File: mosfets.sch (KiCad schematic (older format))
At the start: 51 parts, among them J11 Conn_01x02, J12 Conn_01x02, J13 Conn_01x02, J14 Conn_01x02, J16 Conn_01x02, J17 Conn_01x02, J18 Conn_01x02, J19 Conn_01x02, J20 Conn_01x02, J44 Conn_01x02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

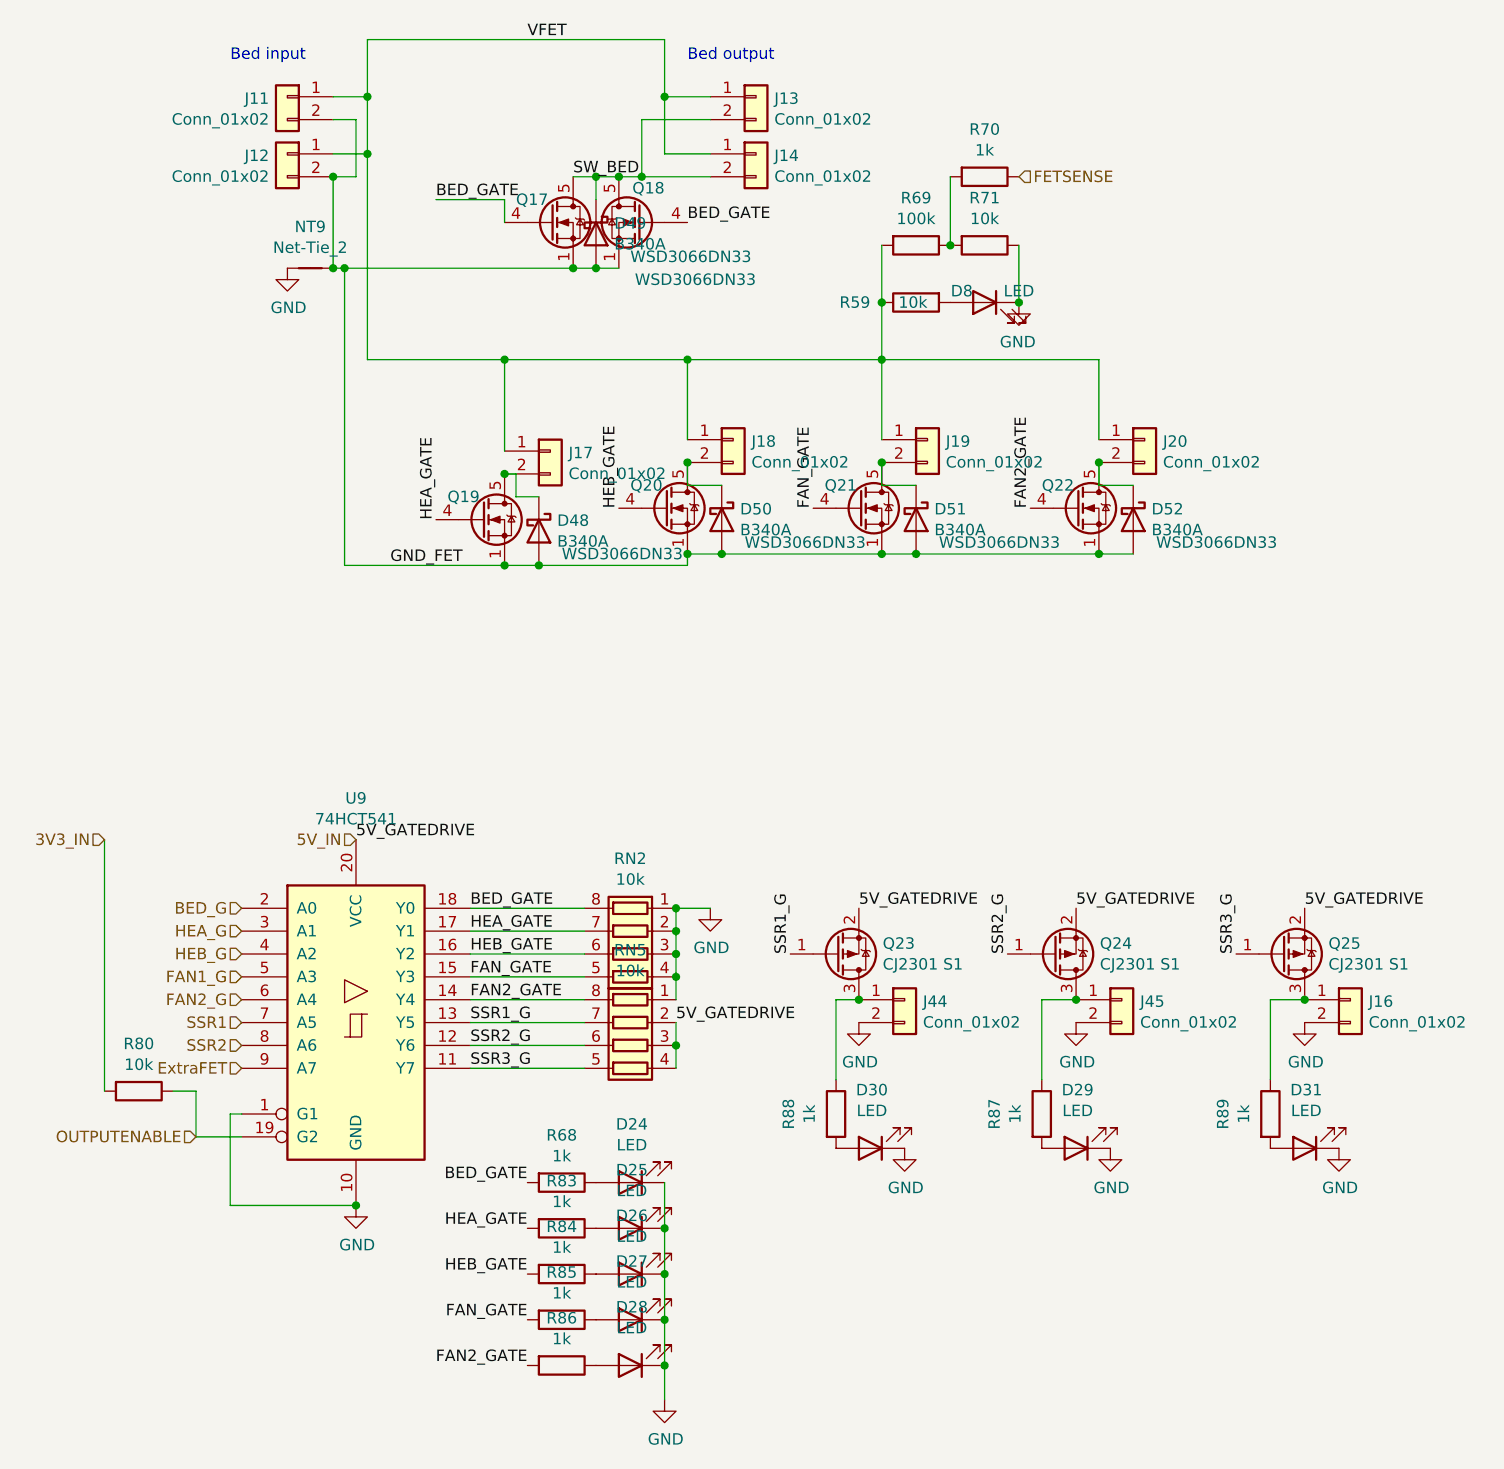
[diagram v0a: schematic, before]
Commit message: Add pfet to switch vfet positive rail and nfet to switch pfet for emergency heater poweroff.
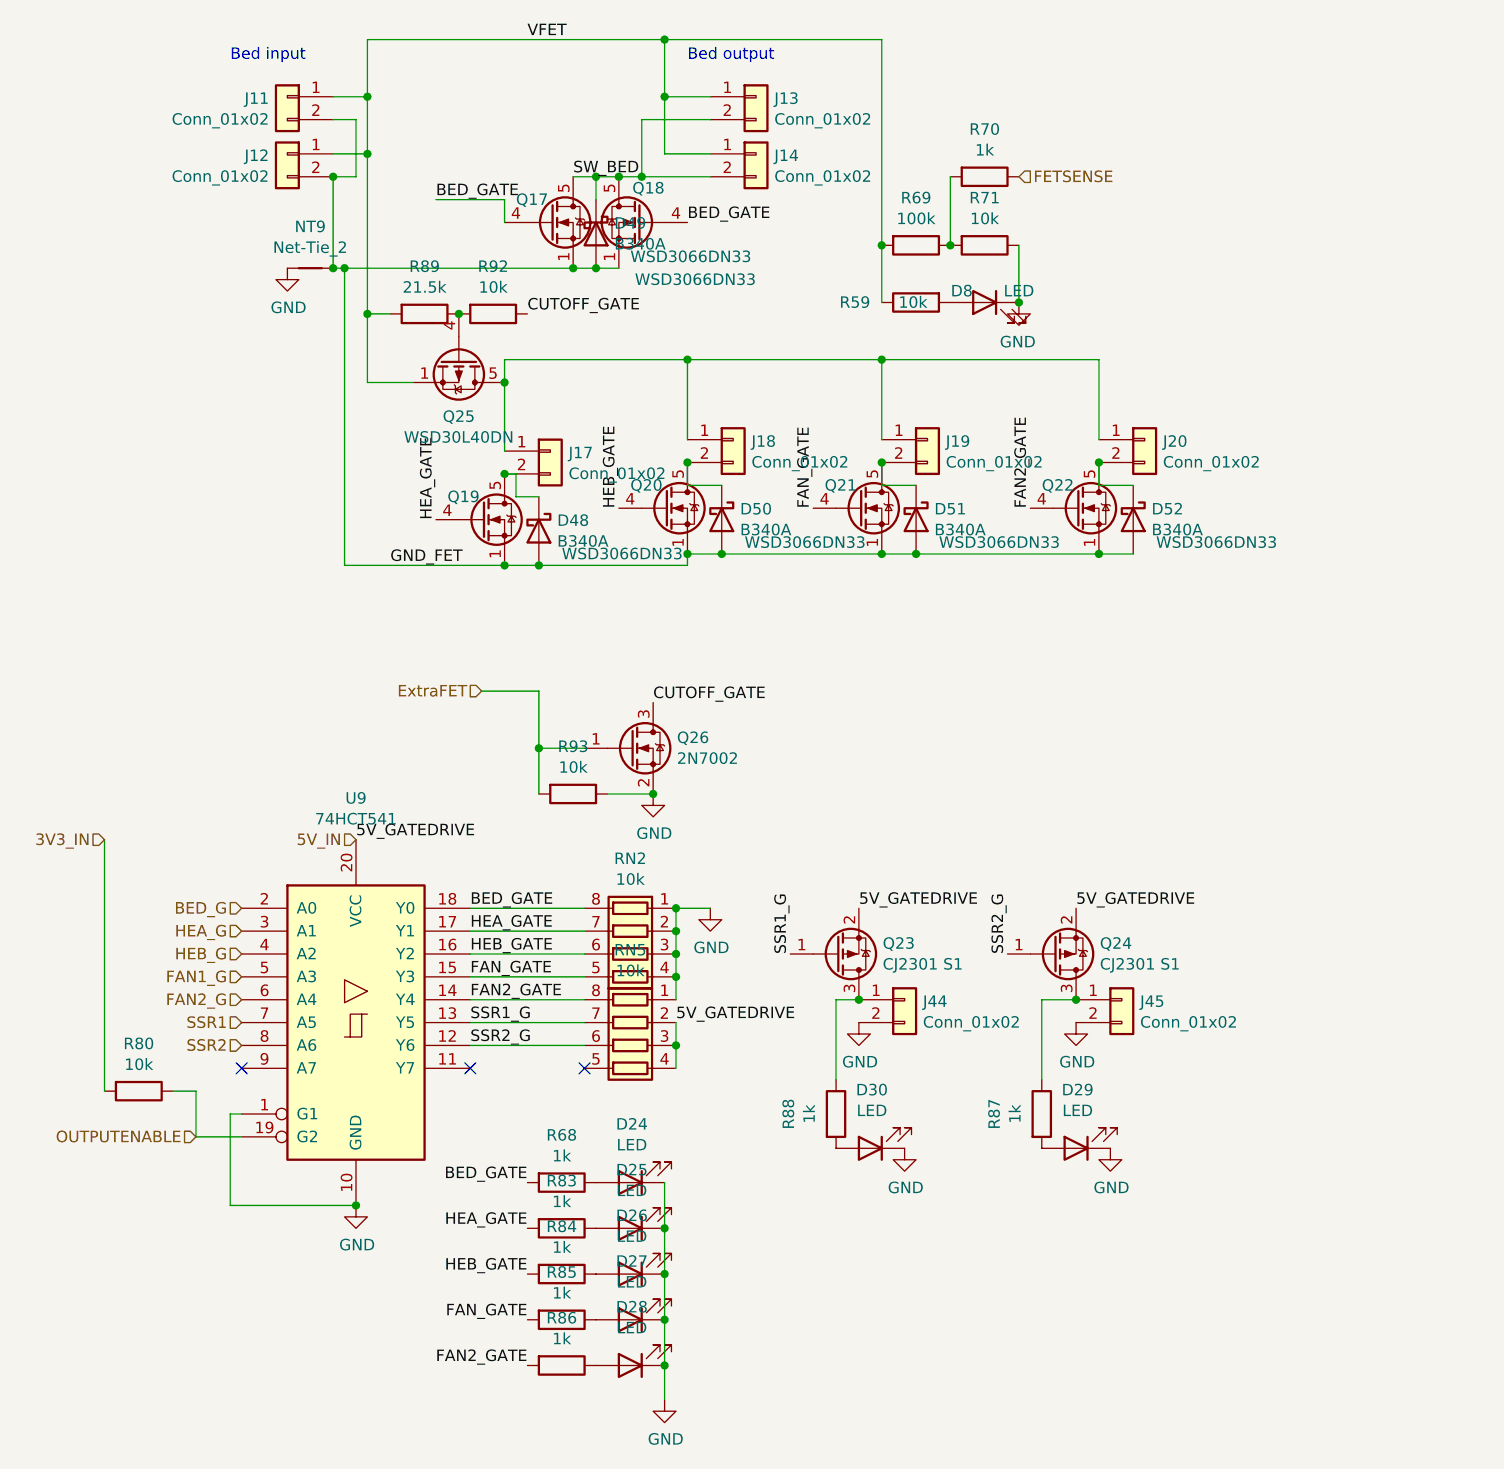
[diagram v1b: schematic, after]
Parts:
- removed D31: LED, LED_SMD:LED_0603_1608Metric, symbol Device:LED
- removed J16: Conn_01x02, Connector_PinHeader_2.54mm:PinHeader_1x02_P2.54mm_Vertical, symbol Connector_Generic:Conn_01x02
- removed Q25: CJ2301 S1, Package_TO_SOT_SMD:SOT-23, symbol Transistor_FET:AO3401A
- added Q25: WSD30L40DN, Package_SO:Vishay_PowerPAK_1212-8_Single, symbol Transistor_FET:SiS415DNT
- added Q26: 2N7002, Package_TO_SOT_SMD:SOT-23, symbol Transistor_FET:2N7002
- added R92, R93: 10k, Resistor_SMD:R_0402_1005Metric, symbol Device:R
- R89: value 1k -> 21.5k
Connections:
- net ExtraFET: now also Q26.1 (G), R93.2; no longer U9.9 (A7)
- net GND: now also Q26.2 (S), R93.1
- net VFET: now also R89.2, Q25.1 (S), Q25.2 (S), Q25.3 (S); no longer J17.1 (Pin_1), J18.1 (Pin_1), J19.1 (Pin_1), J20.1 (Pin_1)
- net at R89.1: now also Q25.4 (G), R92.2
- net SSR3_G: no longer names the net of U9.11 (Y7)
- net SSR3_G: no longer RN5.5 (R4.2)
- new net: J17.1 (Pin_1), J18.1 (Pin_1), J19.1 (Pin_1), J20.1 (Pin_1), Q25.5 (D)
- new net CUTOFF_GATE: Q26.3 (D), R92.1
- no-connect marks 0 -> 3
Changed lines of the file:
@@
 	3400 2600 2600 2600
 Wire Wire Line
-	2600 3000 2600 2600
+	2600 3000 2600 2700
 Wire Wire Line
 	2600 3500 2750 3500
@@
 Text HLabel 1450 5600 0    50   Input ~ 0
 SSR2
-Text HLabel 1450 5700 0    50   Input ~ 0
+Text HLabel 2500 4050 0    50   Input ~ 0
 ExtraFET
 Wire Wire Line
@@
 Wire Wire Line
 	2950 5600 2450 5600
-Wire Wire Line
-	2950 5700 2450 5700
 $Comp
 L Device:R R?
@@
 	-1   0    0    -1
 $EndComp
-Wire Wire Line
-	4250 2350 4250 2600
 $Comp
 L Device:R R69
@@
 Wire Wire Line
 	4250 2100 4250 2350
-Connection ~ 4250 2350
 $Comp
 L Device:R R70
@@
 Wire Wire Line
 	1900 2200 2900 2200
-Wire Wire Line
-	2600 2600 2000 2600
-Wire Wire Line
-	2000 2600 2000 1700
-Connection ~ 2600 2600
 Connection ~ 2000 1700
 Text Label 2700 1200 0    50   ~ 0
@@
 Text Label 2100 3500 0    50   ~ 0
 GND_FET
-$Comp
-L Transistor_FET:AO3401A Q25
-U 1 1 65BEA16F
-P 6000 5200
-F 0 "Q25" H 6204 5154 50  0000 L CNN
-F 1 "CJ2301 S1" H 6204 5245 50  0000 L CNN
-F 2 "Package_TO_SOT_SMD:SOT-23" H 6200 5125 50  0001 L CIN
-F 3 "http://www.aosmd.com/pdfs/datasheet/AO3401A.pdf" H 6000 5200 50  0001 L CNN
-	1    6000 5200
-	1    0    0    1
-$EndComp
-Text Label 6100 5000 0    50   ~ 0
-5V_GATEDRIVE
-$Comp
-L Connector_Generic:Conn_01x02 J?
-U 1 1 65BEA31E
-P 6300 5400
-AR Path="/65BEA31E" Ref="J?"  Part="1"
-AR Path="/612538A5/65BEA31E" Ref="J16"  Part="1"
-F 0 "J16" H 6380 5392 50  0000 L CNN
-F 1 "Conn_01x02" H 6380 5301 50  0000 L CNN
-F 2 "Connector_PinHeader_2.54mm:PinHeader_1x02_P2.54mm_Vertical" H 6300 5400 50  0001 C CNN
-F 3 "~" H 6300 5400 50  0001 C CNN
-	1    6300 5400
-	1    0    0    -1
-$EndComp
-$Comp
-L power:GND #PWR08
-U 1 1 65BEA328
-P 6100 5500
-F 0 "#PWR08" H 6100 5250 50  0001 C CNN
-F 1 "GND" H 6105 5327 50  0000 C CNN
-F 2 "" H 6100 5500 50  0001 C CNN
-F 3 "" H 6100 5500 50  0001 C CNN
-	1    6100 5500
-	1    0    0    -1
-$EndComp
-Text Label 5800 5200 1    50   ~ 0
-SSR3_G
-Text Label 2450 5700 0    50   ~ 0
-SSR3_G
 Text Label 2700 6200 2    50   ~ 0
 BED_GATE
@@
 	4050 5400 4050 5750
 Connection ~ 4150 5400
-$Comp
-L Device:R R89
-U 1 1 60EB4240
-P 5950 5900
-F 0 "R89" V 5743 5900 50  0000 C CNN
-F 1 "1k" V 5834 5900 50  0000 C CNN
-F 2 "Resistor_SMD:R_0402_1005Metric" V 5880 5900 50  0001 C CNN
-F 3 "~" H 5950 5900 50  0001 C CNN
-	1    5950 5900
-	1    0    0    -1
-$EndComp
-$Comp
-L Device:LED D31
-U 1 1 60EB44E2
-P 6100 6050
-F 0 "D31" H 6093 5795 50  0000 C CNN
-F 1 "LED" H 6093 5886 50  0000 C CNN
-F 2 "LED_SMD:LED_0603_1608Metric" H 6100 6050 50  0001 C CNN
-F 3 "~" H 6100 6050 50  0001 C CNN
-	1    6100 6050
-	-1   0    0    1
-$EndComp
-$Comp
-L power:GND #PWR067
-U 1 1 60EB44EC
-P 6250 6050
-F 0 "#PWR067" H 6250 5800 50  0001 C CNN
-F 1 "GND" H 6255 5877 50  0000 C CNN
-F 2 "" H 6250 6050 50  0001 C CNN
-F 3 "" H 6250 6050 50  0001 C CNN
-	1    6250 6050
-	1    0    0    -1
-$EndComp
-Wire Wire Line
-	6100 5400 5950 5400
-Wire Wire Line
-	5950 5400 5950 5750
-Connection ~ 6100 5400
 Wire Wire Line
 	3350 5700 3350 5600
@@
 Wire Wire Line
 	3000 2200 2900 2200
+NoConn ~ 1450 5700
+Wire Wire Line
+	4250 2100 4250 1200
+Wire Wire Line
+	4250 1200 3300 1200
+Connection ~ 4250 2100
+Connection ~ 3300 1200
+$Comp
+L Transistor_FET:SiS415DNT Q25
+U 1 1 610823DA
+P 2400 2600
+F 0 "Q25" V 2649 2600 50  0000 C CNN
+F 1 "WSD30L40DN" V 2740 2600 50  0000 C CNN
+F 2 "Package_SO:Vishay_PowerPAK_1212-8_Single" H 2600 2525 50  0001 L CIN
+F 3 "https://www.vishay.com/docs/63684/sis415dnt.pdf" V 2400 2600 50  0001 L CNN
+	1    2400 2600
+	0    1    1    0
+$EndComp
+Connection ~ 2600 2700
+Wire Wire Line
+	2600 2700 2600 2600
+Wire Wire Line
+	2200 2700 2000 2700
+Wire Wire Line
+	2000 1700 2000 2400
+$Comp
+L Device:R R89
+U 1 1 6108A26A
+P 2250 2400
+F 0 "R89" V 2043 2400 50  0000 C CNN
+F 1 "21.5k" V 2134 2400 50  0000 C CNN
+F 2 "Resistor_SMD:R_0402_1005Metric" V 2180 2400 50  0001 C CNN
+F 3 "~" H 2250 2400 50  0001 C CNN
+	1    2250 2400
+	0    1    1    0
+$EndComp
+Wire Wire Line
+	2100 2400 2000 2400
+Connection ~ 2000 2400
+Wire Wire Line
+	2000 2400 2000 2700
+Text Label 2700 2400 0    50   ~ 0
+CUTOFF_GATE
+Text Label 3250 4100 0    50   ~ 0
+CUTOFF_GATE
+$Comp
+L Device:R R92
+U 1 1 610A49E0
+P 2550 2400
+F 0 "R92" V 2343 2400 50  0000 C CNN
+F 1 "10k" V 2434 2400 50  0000 C CNN
+F 2 "Resistor_SMD:R_0402_1005Metric" V 2480 2400 50  0001 C CNN
+F 3 "~" H 2550 2400 50  0001 C CNN
+	1    2550 2400
+	0    1    1    0
+$EndComp
+Connection ~ 2400 2400
+NoConn ~ 2950 5700
+NoConn ~ 2450 5700
+$Comp
+L Transistor_FET:2N7002 Q26
+U 1 1 610B28F1
+P 3150 4300
+F 0 "Q26" H 3354 4346 50  0000 L CNN
+F 1 "2N7002" H 3354 4255 50  0000 L CNN
+F 2 "Package_TO_SOT_SMD:SOT-23" H 3350 4225 50  0001 L CIN
+F 3 "https://www.onsemi.com/pub/Collateral/NDS7002A-D.PDF" H 3150 4300 50  0001 L CNN
+	1    3150 4300
+	1    0    0    -1
+$EndComp
+$Comp
+L power:GND #PWR08
+U 1 1 610B5CC2
+P 3250 4500
+F 0 "#PWR08" H 3250 4250 50  0001 C CNN
+F 1 "GND" H 3255 4327 50  0000 C CNN
+F 2 "" H 3250 4500 50  0001 C CNN
+F 3 "" H 3250 4500 50  0001 C CNN
+	1    3250 4500
+	1    0    0    -1
+$EndComp
+$Comp
+L Device:R R93
+U 1 1 610B7D0D
+P 2900 4500
+F 0 "R93" V 2693 4500 50  0000 C CNN
+F 1 "10k" V 2784 4500 50  0000 C CNN
+F 2 "Resistor_SMD:R_0402_1005Metric" V 2830 4500 50  0001 C CNN
+F 3 "~" H 2900 4500 50  0001 C CNN
+	1    2900 4500
+	0    1    1    0
+$EndComp
+Wire Wire Line
+	2950 4300 2750 4300
+Wire Wire Line
+	2750 4300 2750 4500
+Wire Wire Line
+	3250 4500 3050 4500
+Connection ~ 3250 4500
+Wire Wire Line
+	2500 4050 2750 4050
+Wire Wire Line
+	2750 4050 2750 4300
+Connection ~ 2750 4300
 $EndSCHEMATC

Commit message: Fix FPs for U4 and U9
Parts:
- U9: footprint Package_SO:TSSOP-20_4.4x5mm_P0.5mm -> Package_SO:TSSOP-20_4.4x6.5mm_P0.65mm
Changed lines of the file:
@@
 F 0 "U9" H 1950 6481 50  0000 C CNN
 F 1 "74HCT541" H 1950 6390 50  0000 C CNN
-F 2 "Package_SO:TSSOP-20_4.4x5mm_P0.5mm" H 1950 5500 50  0001 C CNN
+F 2 "Package_SO:TSSOP-20_4.4x6.5mm_P0.65mm" H 1950 5500 50  0001 C CNN
 F 3 "http://www.ti.com/lit/gpn/sn74HCT541" H 1950 5500 50  0001 C CNN
 	1    1950 5500

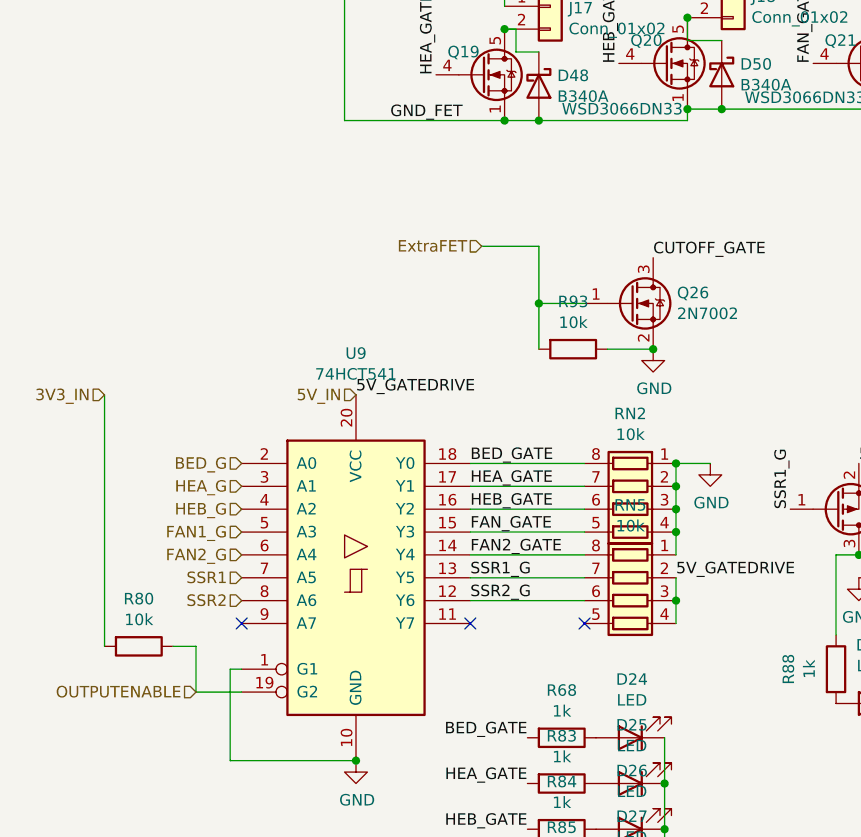
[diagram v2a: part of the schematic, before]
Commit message: Switch ADC opamp to 5V Add 4.7k series resistors (RN9) to thermistor inputs. Add 10k pulldowns (RN8) to FET gate driver inputs.
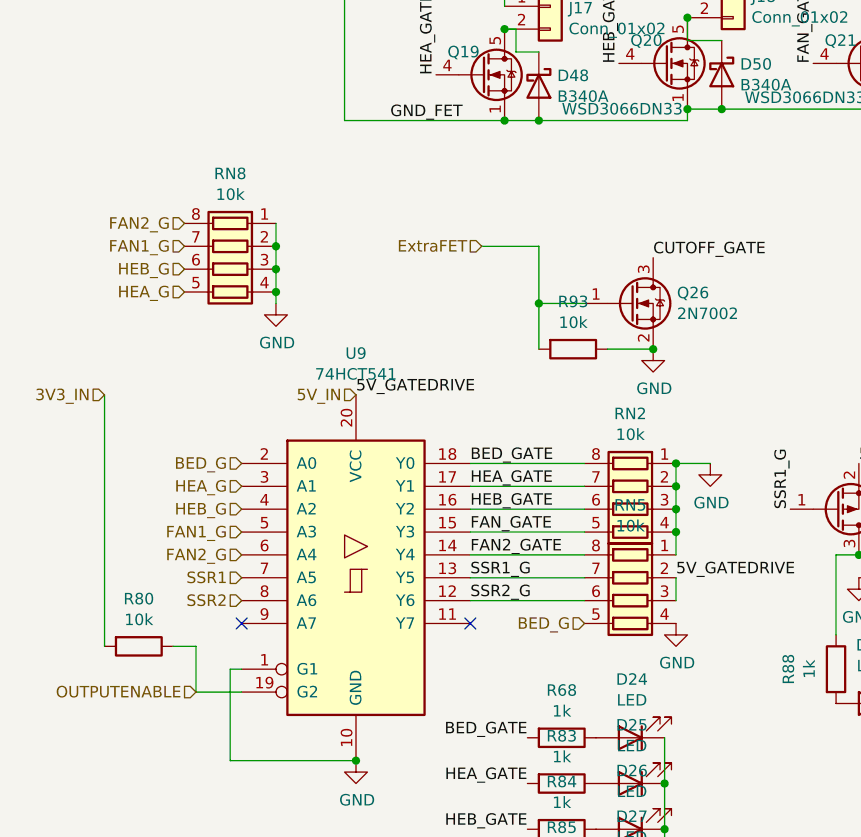
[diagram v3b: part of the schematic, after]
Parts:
- added RN8: 10k, Resistor_SMD:R_Array_Concave_4x0603, symbol Device:R_Pack04
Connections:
- net 5V_IN: no longer RN5.4 (R4.1)
- net BED_G: now also RN5.5 (R4.2)
- net FAN1_G: now also RN8.7 (R2.2)
- net FAN2_G: now also RN8.8 (R1.2)
- net GND: now also RN5.4 (R4.1), RN8.1 (R1.1), RN8.2 (R2.1), RN8.3 (R3.1), RN8.4 (R4.1)
- net HEA_G: now also RN8.5 (R4.2)
- net HEB_G: now also RN8.6 (R3.2)
- no-connect marks 3 -> 2
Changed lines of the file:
@@
 Connection ~ 4150 5400
 Wire Wire Line
-	3350 5700 3350 5600
-Wire Wire Line
 	3350 5500 3350 5600
-Connection ~ 3350 5600
 $Comp
 L Device:R_Pack04 RN5
@@
 $EndComp
 Connection ~ 2400 2400
-NoConn ~ 2950 5700
 NoConn ~ 2450 5700
 $Comp
@@
 	2750 4050 2750 4300
 Connection ~ 2750 4300
+$Comp
+L power:GND #PWR0152
+U 1 1 61B81538
+P 3350 5700
+F 0 "#PWR0152" H 3350 5450 50  0001 C CNN
+F 1 "GND" H 3355 5527 50  0000 C CNN
+F 2 "" H 3350 5700 50  0001 C CNN
+F 3 "" H 3350 5700 50  0001 C CNN
+	1    3350 5700
+	1    0    0    -1
+$EndComp
+Text HLabel 2950 5700 0    50   Input ~ 0
+BED_G
+$Comp
+L Device:R_Pack04 RN8
+U 1 1 61B8A880
+P 1400 4150
+F 0 "RN8" V 983 4150 50  0000 C CNN
+F 1 "10k" V 1074 4150 50  0000 C CNN
+F 2 "Resistor_SMD:R_Array_Concave_4x0603" V 1675 4150 50  0001 C CNN
+F 3 "~" H 1400 4150 50  0001 C CNN
+	1    1400 4150
+	0    -1   1    0
+$EndComp
+$Comp
+L power:GND #PWR067
+U 1 1 61B8B3E4
+P 1600 4300
+F 0 "#PWR067" H 1600 4050 50  0001 C CNN
+F 1 "GND" H 1605 4127 50  0000 C CNN
+F 2 "" H 1600 4300 50  0001 C CNN
+F 3 "" H 1600 4300 50  0001 C CNN
+	1    1600 4300
+	1    0    0    -1
+$EndComp
+Wire Wire Line
+	1600 3950 1600 4050
+Connection ~ 1600 4050
+Wire Wire Line
+	1600 4050 1600 4150
+Connection ~ 1600 4150
+Wire Wire Line
+	1600 4150 1600 4250
+Connection ~ 1600 4250
+Wire Wire Line
+	1600 4250 1600 4300
+Text HLabel 1200 3950 0    50   Input ~ 0
+FAN2_G
+Text HLabel 1200 4050 0    50   Input ~ 0
+FAN1_G
+Text HLabel 1200 4150 0    50   Input ~ 0
+HEB_G
+Text HLabel 1200 4250 0    50   Input ~ 0
+HEA_G
 $EndSCHEMATC
